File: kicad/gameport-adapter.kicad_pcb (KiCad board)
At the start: 2 copper layers, 45.7 x 39.4 mm, 8 parts, among them SW1 SW_DIP_x04, U1 Arduino_Pro_Micro

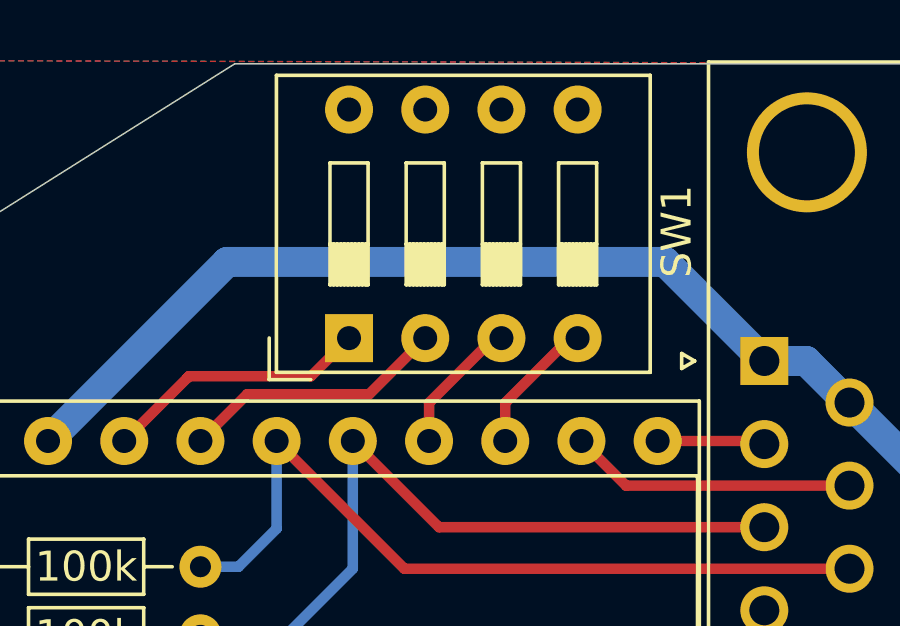
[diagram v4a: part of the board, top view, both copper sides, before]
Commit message: Rotated switch order
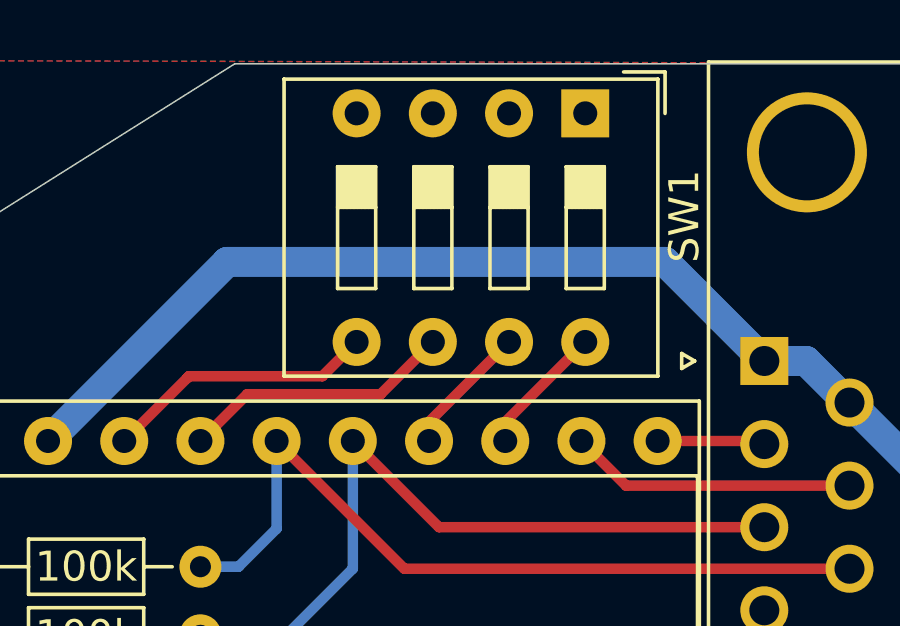
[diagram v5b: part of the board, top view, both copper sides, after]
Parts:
- moved SW1 10.9 mm to (105.7, 70.2), turned to 270 degrees
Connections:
- SW1 pad 1: SW1 -> GND
- SW1 pad 2: SW2 -> GND
- SW1 pad 3: SW3 -> GND
- SW1 pad 4: SW4 -> GND
- SW1 pad 5: GND -> SW4
- SW1 pad 6: GND -> SW3
- SW1 pad 7: GND -> SW2
- SW1 pad 8: GND -> SW1
- U1 pad 15: SW4 -> SW1
- U1 pad 16: SW3 -> SW2
- U1 pad 19: SW2 -> SW3
- U1 pad 20: SW1 -> SW4
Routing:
- net SW4: track 4.32 -> 9.20 mm
- net SW3: track 4.32 -> 9.11 mm
- net SW1: track 9.00 -> 4.41 mm
- net SW2: track 8.91 -> 4.41 mm
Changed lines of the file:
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@@
     (add_net MIDI_RXD)
     (add_net MIDI_TXD)
+    (add_net "Net-(U1-Pad1)")
+    (add_net "Net-(U1-Pad2)")
+    (add_net "Net-(U1-Pad22)")
+    (add_net "Net-(U1-Pad24)")
+    (add_net "Net-(U1-Pad5)")
+    (add_net "Net-(U1-Pad6)")
     (add_net SW1)
     (add_net SW2)
@@
       (net 9 AxisY_1))
     (pad 20 thru_hole oval (at 15.24 10.16 90) (size 1.6 1.6) (drill 0.8) (layers *.Cu *.Mask)
-      (net 15 SW1))
+      (net 16 SW4))
     (pad 8 thru_hole oval (at 0 17.78 90) (size 1.6 1.6) (drill 0.8) (layers *.Cu *.Mask)
       (net 12 MIDI_TXD))
     (pad 19 thru_hole oval (at 15.24 12.7 90) (size 1.6 1.6) (drill 0.8) (layers *.Cu *.Mask)
-      (net 14 SW2))
+      (net 13 SW3))
     (pad 7 thru_hole oval (at 0 15.24 90) (size 1.6 1.6) (drill 0.8) (layers *.Cu *.Mask)
       (net 5 AxisY_2))
@@
     (pad 5 thru_hole oval (at 0 10.16 90) (size 1.6 1.6) (drill 0.8) (layers *.Cu *.Mask))
     (pad 16 thru_hole oval (at 15.24 20.32 90) (size 1.6 1.6) (drill 0.8) (layers *.Cu *.Mask)
-      (net 13 SW3))
+      (net 14 SW2))
     (pad 4 thru_hole oval (at 0 7.62 90) (size 1.6 1.6) (drill 0.8) (layers *.Cu *.Mask)
       (net 2 GND))
     (pad 15 thru_hole oval (at 15.24 22.86 90) (size 1.6 1.6) (drill 0.8) (layers *.Cu *.Mask)
-      (net 16 SW4))
+      (net 15 SW1))
     (pad 3 thru_hole oval (at 0 5.08 90) (size 1.6 1.6) (drill 0.8) (layers *.Cu *.Mask)
       (net 2 GND))
@@
   )
   (module Button_Switch_THT:SW_DIP_SPSTx04_Slide_9.78x12.34mm_W7.62mm_P2.54mm (layer F.Cu)
-    (at 97.79 77.724 90)
+    (at 105.664 70.231 270)
     (descr "4x-dip-switch SPST , Slide, row spacing 7.62 mm (300 mils), body size 9.78x12.34mm (see e.g. https://www.ctscorp.com/wp-content/uploads/206-208.pdf)")
     (tags "DIP Switch SPST Slide 7.62mm 300mil")
-    (fp_text reference SW1 (at 3.556 10.922 90) (layer F.SilkS)
+    (fp_text reference SW1 (at 3.429 -3.302 90) (layer F.SilkS)
       (effects (font (size 1 1) (thickness 0.15)))
     )
@@
       (effects (font (size 0.8 0.8) (thickness 0.12)))
     )
-    (pad 8 thru_hole oval (at 7.62 0 90) (size 1.6 1.6) (drill 0.8) (layers *.Cu *.Mask)
-      (net 2 GND))
-    (pad 4 thru_hole oval (at 0 7.62 90) (size 1.6 1.6) (drill 0.8) (layers *.Cu *.Mask)
+    (pad 8 thru_hole oval (at 7.62 0 270) (size 1.6 1.6) (drill 0.8) (layers *.Cu *.Mask)
+      (net 15 SW1))
+    (pad 4 thru_hole oval (at 0 7.62 270) (size 1.6 1.6) (drill 0.8) (layers *.Cu *.Mask)
+      (net 2 GND))
+    (pad 7 thru_hole oval (at 7.62 2.54 270) (size 1.6 1.6) (drill 0.8) (layers *.Cu *.Mask)
+      (net 14 SW2))
+    (pad 3 thru_hole oval (at 0 5.08 270) (size 1.6 1.6) (drill 0.8) (layers *.Cu *.Mask)
+      (net 2 GND))
+    (pad 6 thru_hole oval (at 7.62 5.08 270) (size 1.6 1.6) (drill 0.8) (layers *.Cu *.Mask)
+      (net 13 SW3))
+    (pad 2 thru_hole oval (at 0 2.54 270) (size 1.6 1.6) (drill 0.8) (layers *.Cu *.Mask)
+      (net 2 GND))
+    (pad 5 thru_hole oval (at 7.62 7.62 270) (size 1.6 1.6) (drill 0.8) (layers *.Cu *.Mask)
       (net 16 SW4))
-    (pad 7 thru_hole oval (at 7.62 2.54 90) (size 1.6 1.6) (drill 0.8) (layers *.Cu *.Mask)
-      (net 2 GND))
-    (pad 3 thru_hole oval (at 0 5.08 90) (size 1.6 1.6) (drill 0.8) (layers *.Cu *.Mask)
-      (net 13 SW3))
-    (pad 6 thru_hole oval (at 7.62 5.08 90) (size 1.6 1.6) (drill 0.8) (layers *.Cu *.Mask)
-      (net 2 GND))
-    (pad 2 thru_hole oval (at 0 2.54 90) (size 1.6 1.6) (drill 0.8) (layers *.Cu *.Mask)
-      (net 14 SW2))
-    (pad 5 thru_hole oval (at 7.62 7.62 90) (size 1.6 1.6) (drill 0.8) (layers *.Cu *.Mask)
-      (net 2 GND))
-    (pad 1 thru_hole rect (at 0 0 90) (size 1.6 1.6) (drill 0.8) (layers *.Cu *.Mask)
-      (net 15 SW1))
+    (pad 1 thru_hole rect (at 0 0 270) (size 1.6 1.6) (drill 0.8) (layers *.Cu *.Mask)
+      (net 2 GND))
     (model ${KISYS3DMOD}/Button_Switch_THT.3dshapes/SW_DIP_SPSTx04_Slide_9.78x12.34mm_W7.62mm_P2.54mm.wrl
       (at (xyz 0 0 0))
@@
   (segment (start 101.981 92.329) (end 101.981 88.269997) (width 0.35) (layer B.Cu) (net 12))
   (via (at 101.976003 88.265) (size 0.8) (drill 0.4) (layers F.Cu B.Cu) (net 12))
-  (segment (start 100.457 79.883) (end 100.457 81.153) (width 0.35) (layer F.Cu) (net 13))
-  (segment (start 102.616 77.724) (end 100.457 79.883) (width 0.35) (layer F.Cu) (net 13))
-  (segment (start 94.395989 79.594011) (end 92.837 81.153) (width 0.35) (layer F.Cu) (net 14))
-  (segment (start 98.459989 79.594011) (end 94.395989 79.594011) (width 0.35) (layer F.Cu) (net 14))
-  (segment (start 100.33 77.724) (end 98.459989 79.594011) (width 0.35) (layer F.Cu) (net 14))
-  (segment (start 92.456 78.994) (end 92.3925 79.0575) (width 0.35) (layer F.Cu) (net 15))
-  (segment (start 96.52 78.994) (end 92.456 78.994) (width 0.35) (layer F.Cu) (net 15))
-  (segment (start 97.79 77.724) (end 96.52 78.994) (width 0.35) (layer F.Cu) (net 15))
-  (segment (start 92.456 78.994) (end 90.297 81.153) (width 0.35) (layer F.Cu) (net 15))
-  (segment (start 102.997 79.883) (end 102.997 81.153) (width 0.35) (layer F.Cu) (net 16))
-  (segment (start 105.156 77.724) (end 102.997 79.883) (width 0.35) (layer F.Cu) (net 16))
+  (segment (start 98.840989 79.594011) (end 94.395989 79.594011) (width 0.35) (layer F.Cu) (net 13))
+  (segment (start 94.395989 79.594011) (end 92.837 81.153) (width 0.35) (layer F.Cu) (net 13))
+  (segment (start 100.584 77.851) (end 98.840989 79.594011) (width 0.35) (layer F.Cu) (net 13))
+  (segment (start 100.457 80.518) (end 100.457 81.153) (width 0.35) (layer F.Cu) (net 14))
+  (segment (start 103.124 77.851) (end 100.457 80.518) (width 0.35) (layer F.Cu) (net 14))
+  (segment (start 102.997 80.518) (end 102.997 81.153) (width 0.35) (layer F.Cu) (net 15))
+  (segment (start 105.664 77.851) (end 102.997 80.518) (width 0.35) (layer F.Cu) (net 15))
+  (segment (start 92.456 78.994) (end 92.3925 79.0575) (width 0.35) (layer F.Cu) (net 16))
+  (segment (start 92.456 78.994) (end 90.297 81.153) (width 0.35) (layer F.Cu) (net 16))
+  (segment (start 96.901 78.994) (end 92.456 78.994) (width 0.35) (layer F.Cu) (net 16))
+  (segment (start 98.044 77.851) (end 96.901 78.994) (width 0.35) (layer F.Cu) (net 16))
   (zone (net 2) (net_name GND) (layer F.Cu) (hatch edge 0.508)
     (connect_pads (clearance 0.254))

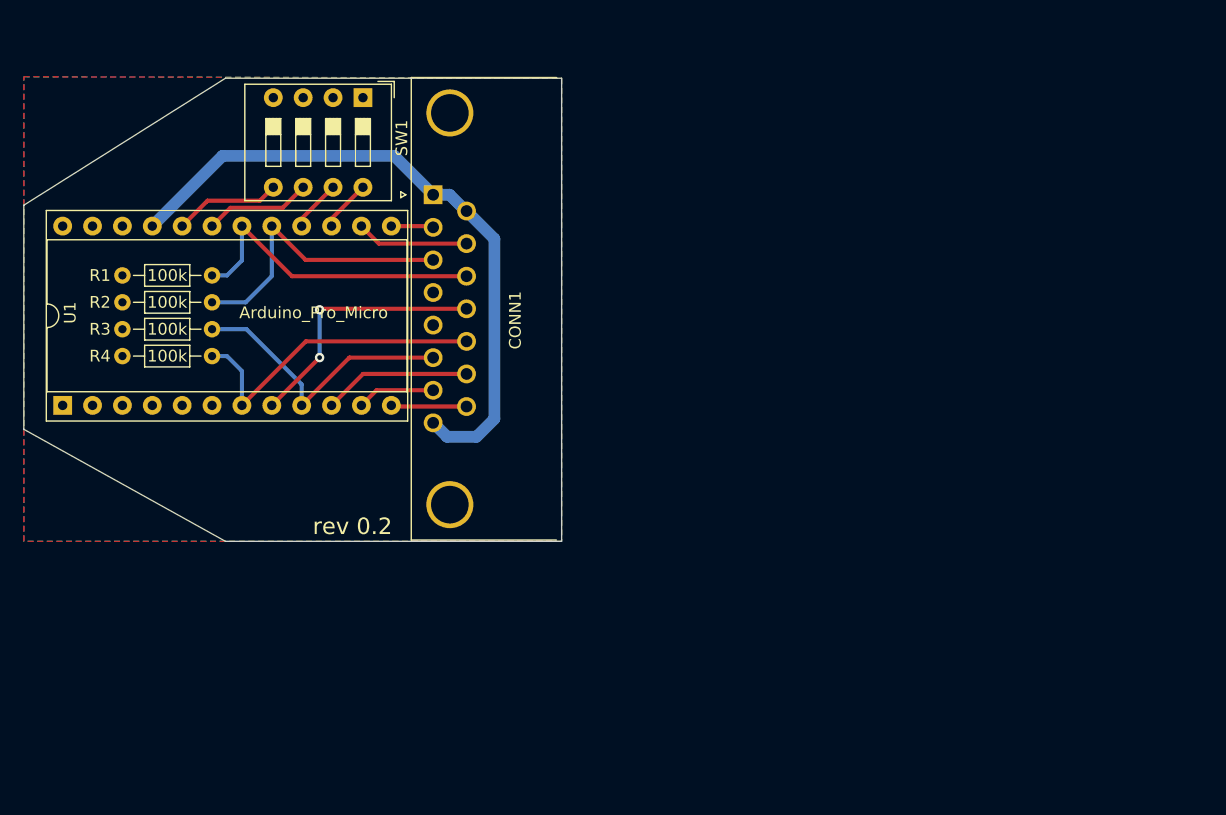
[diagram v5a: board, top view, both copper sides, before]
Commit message: Rev.3 with miniusb and reset button
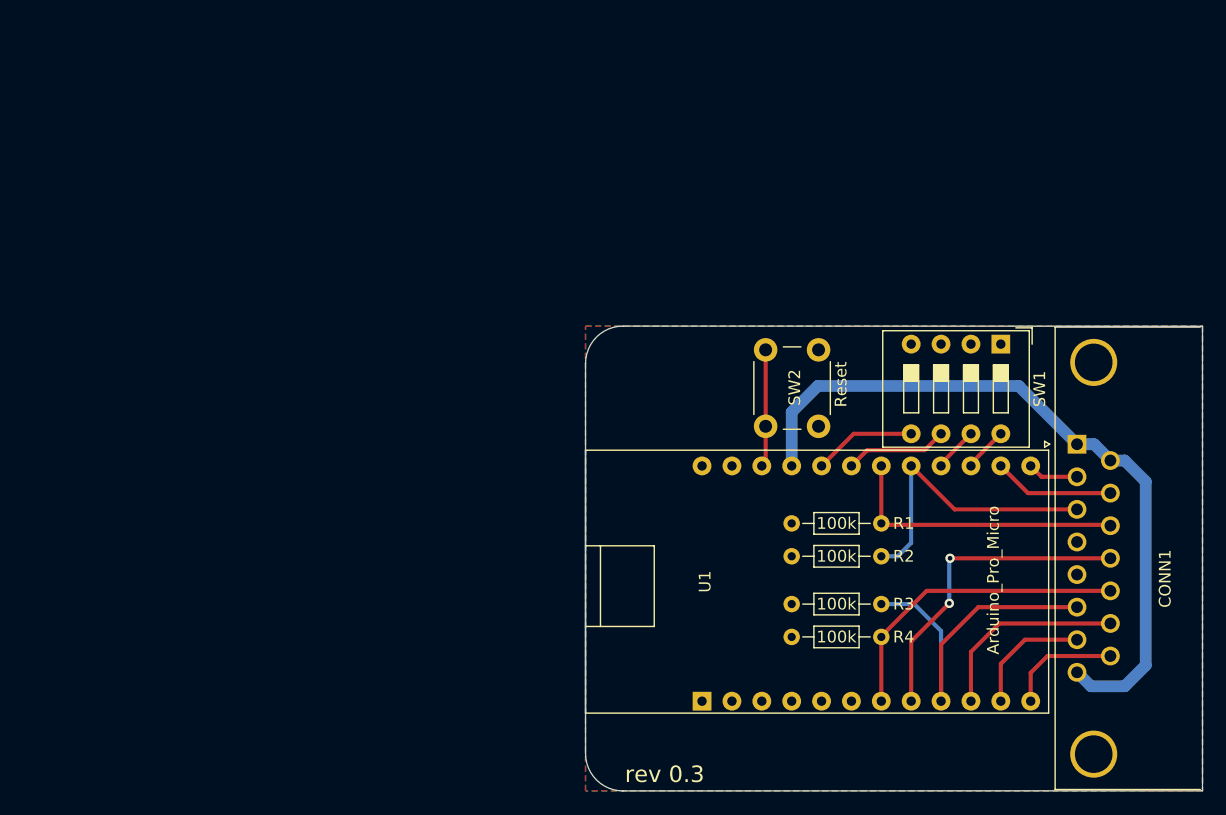
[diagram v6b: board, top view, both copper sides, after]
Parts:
- removed the REF** at (90.9, 75.2)
- added REF**: OSHW-Logo2_9.8x8mm_Copper, Symbol:OSHW-Logo2_9.8x8mm_Copper, F.Cu at (130.0, 95.2)
- added SW2: Reset, Button_Switch_THT:SW_PUSH_6mm, F.Cu at (139.9, 98.2)
- U1: footprint Package_DIP:DIP-24_W15.24mm_Socket -> Necroware:Arduino_Micro_Wide
- moved R4 61.7 mm to (142.1, 116.1)
- moved R3 61.5 mm to (149.7, 113.3)
- moved R2 60.9 mm to (142.1, 109.2)
- moved R1 60.7 mm to (149.7, 106.4)
- moved U1 59.9 mm to (134.5, 121.5)
- moved CONN1 58.7 mm to (166.4, 99.7)
- moved SW1 58.1 mm to (159.9, 91.2)
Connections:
- U1 pad 22: (no net) -> Net-(SW2-Pad1)
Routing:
- net Net-(SW2-Pad1): track 0.00 -> 10.0 mm
- net VCC: track 56.1 -> 61.7 mm
- net AxisY_1: track 24.3 -> 29.7 mm
- net MIDI_TXD: track 22.3 -> 27.2 mm
- net Button_4: track 12.6 -> 17.0 mm
- net Button_2: track 6.63 -> 10.5 mm
- net MIDI_RXD: track 6.44 -> 9.78 mm
- net AxisX_2: track 26.8 -> 24.4 mm
- net AxisY_2: track 27.4 -> 26.6 mm
- net Button_1: track 3.60 -> 4.32 mm
- net Button_3: track 9.55 -> 10.3 mm
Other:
- board size 45.7 x 39.4 mm -> 52.5 x 39.5 mm
- board text added: "github.com/necroware/gameport-adapter"
- board text added: "rev 0.3"
- board text removed: "1"
- board text removed: "15"
- board text removed: "8"
- board text removed: "9"
- board text removed: "rev 0.2"
